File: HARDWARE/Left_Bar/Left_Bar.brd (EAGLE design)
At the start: 138.3 x 28.3 mm, 12 parts

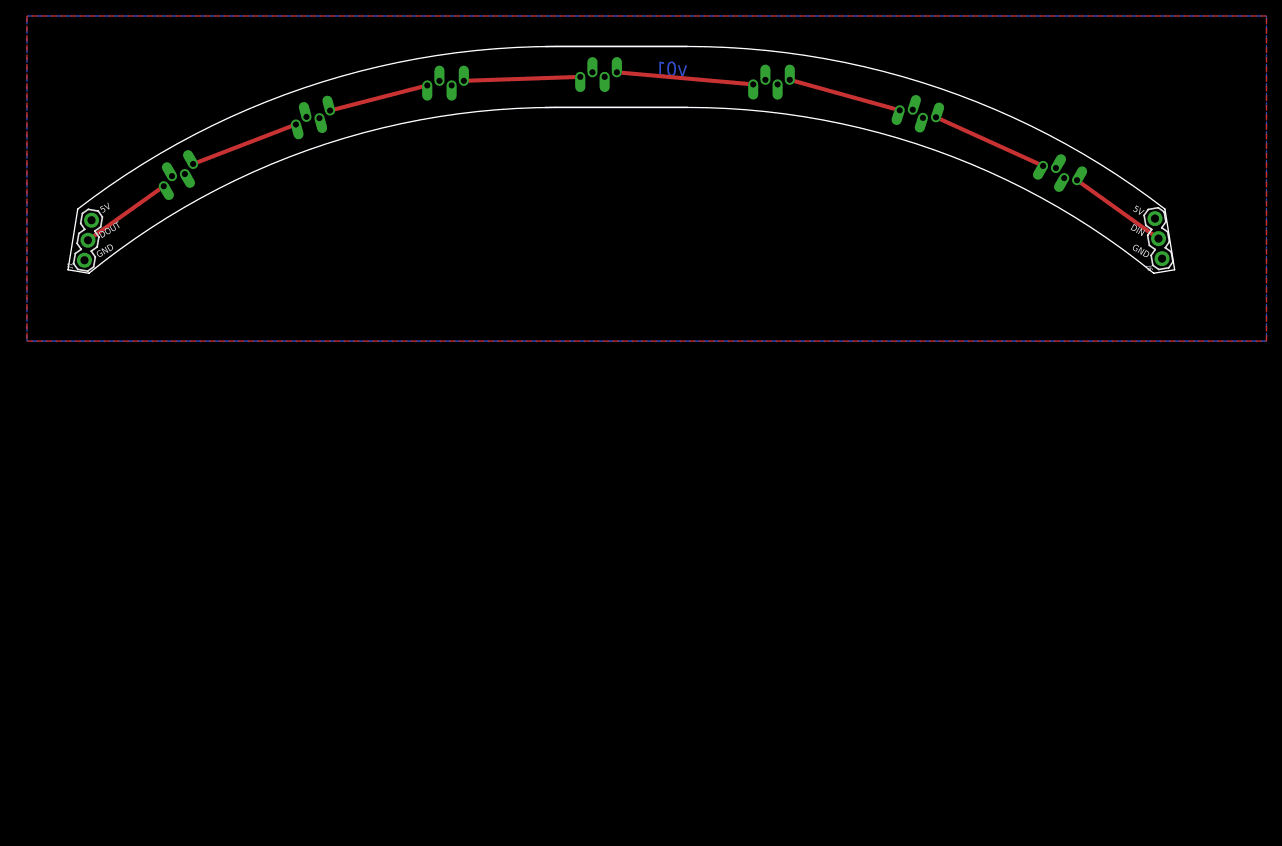
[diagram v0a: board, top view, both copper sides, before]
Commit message: renames right and left, finished left
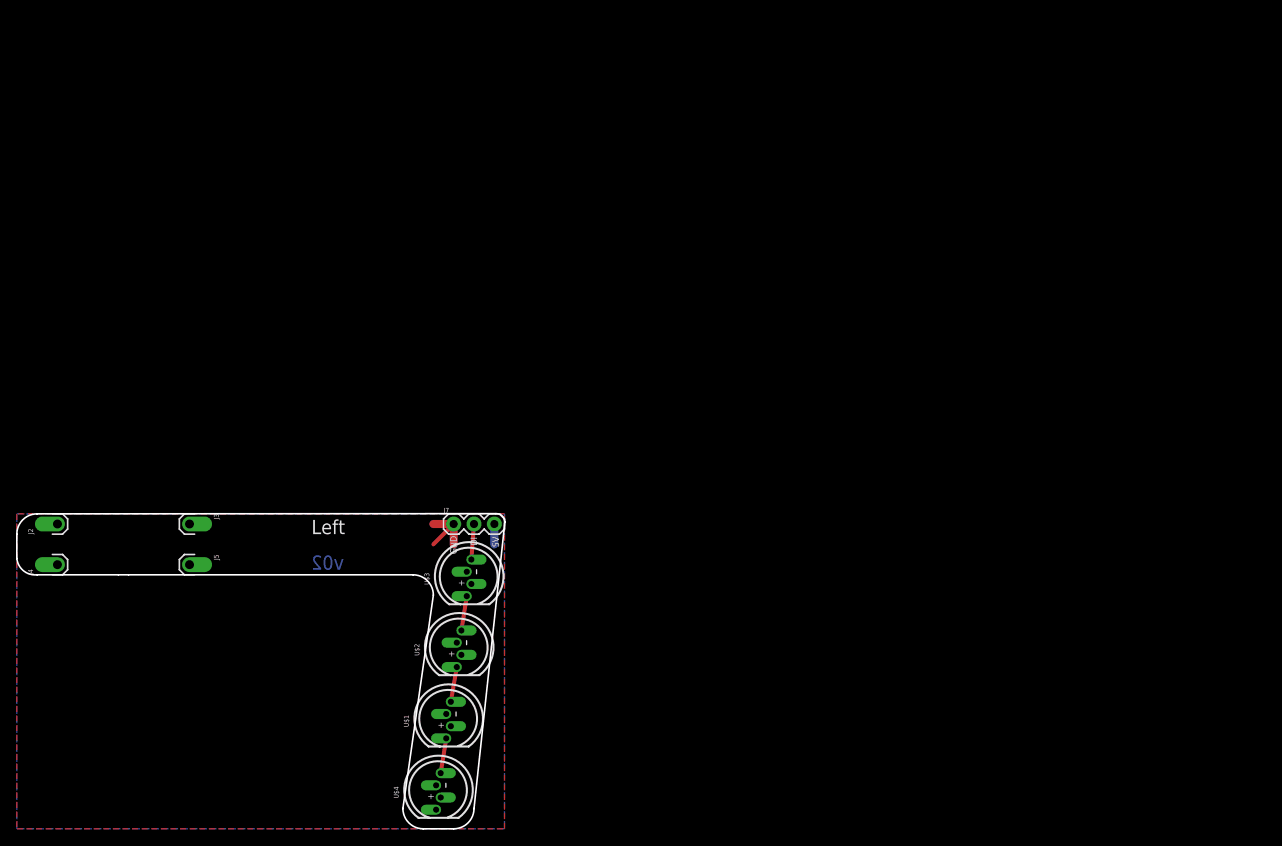
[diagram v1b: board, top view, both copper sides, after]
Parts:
- removed J1, J6: (no value), SparkFun-Connectors:1X03
- removed U$10, U$9: (no value), headsup:SIDE_REF
- removed U$5: (no value), headsup:GLASSES
- removed U$6, U$7, U$8: WS2812B-PTH, SparkFun-LED:WS2812B-PTH-KIT
- added J2, J3, J4, J5: (no value), SparkFun-Connectors:1X01_OFFSET
- added J7: (no value), SparkFun-Connectors:1X03
- moved U$4 92.2 mm to (53.1, 4.55), flipped to the top, turned to 90 degrees
- moved U$1 89.6 mm to (54.3, 13.5), flipped to the top, turned to 90 degrees
- moved U$3 89.6 mm to (56.9, 31.2), flipped to the top, turned to 90 degrees
- moved U$2 88.2 mm to (55.7, 22.4), flipped to the top, turned to 90 degrees
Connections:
- removed net DI: J6.2, U$3.1
- removed net DO: J1.2, U$8.4
- removed net N$3: U$4.4, U$6.1
- removed net N$4: U$6.4, U$7.1
- removed net N$5: U$7.4, U$8.1
- new net DIN: J7.2, U$3.1
- net 5V: now also J7.3; no longer J1.3, J6.3, U$6.2, U$7.2, U$8.2
- net GND: now also J7.1; no longer J1.1, J6.1, U$6.3, U$7.3, U$8.3
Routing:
- net N$3: track 14.6 -> 0.00 mm
- net N$5: track 13.8 -> 0.00 mm
- net N$1: track 17.1 -> 4.40 mm
- net N$4: track 12.6 -> 0.00 mm
- net DI: track 12.5 -> 0.00 mm
- net DO: track 11.6 -> 0.00 mm
- net N$7: track 14.7 -> 4.35 mm
- net N$8: track 14.3 -> 4.41 mm
- net GND: track 0.00 -> 8.67 mm, vias 0 -> 1
- net DIN: track 0.00 -> 4.46 mm
- net 5V: track 0.00 -> 2.54 mm
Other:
- board size 138.3 x 28.3 mm -> 61 x 39.4 mm
- board text added: "DI"
- board text added: "Left"
- board text added: "v02"
- board text removed: "DIN"
- board text removed: "DOUT"
- board text removed: "v01"
